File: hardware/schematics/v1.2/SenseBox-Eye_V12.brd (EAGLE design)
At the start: 61 x 25.4 mm, 103 parts, among them IC1 ESP32-S3-WROOM-1U-N16R8, IC2 WE-CHIP_ESP32-CAM, IC3 MCP73831T-2ACI/OT, IC5 AP2127N-2.8TRG1, IC6 AP2127N-1.5TRG1, IC7 REG710NA-5, IC8 MAX17048, IC9 RP602Z330C-E2-F, J1 USB-C-S, J2 U.FL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

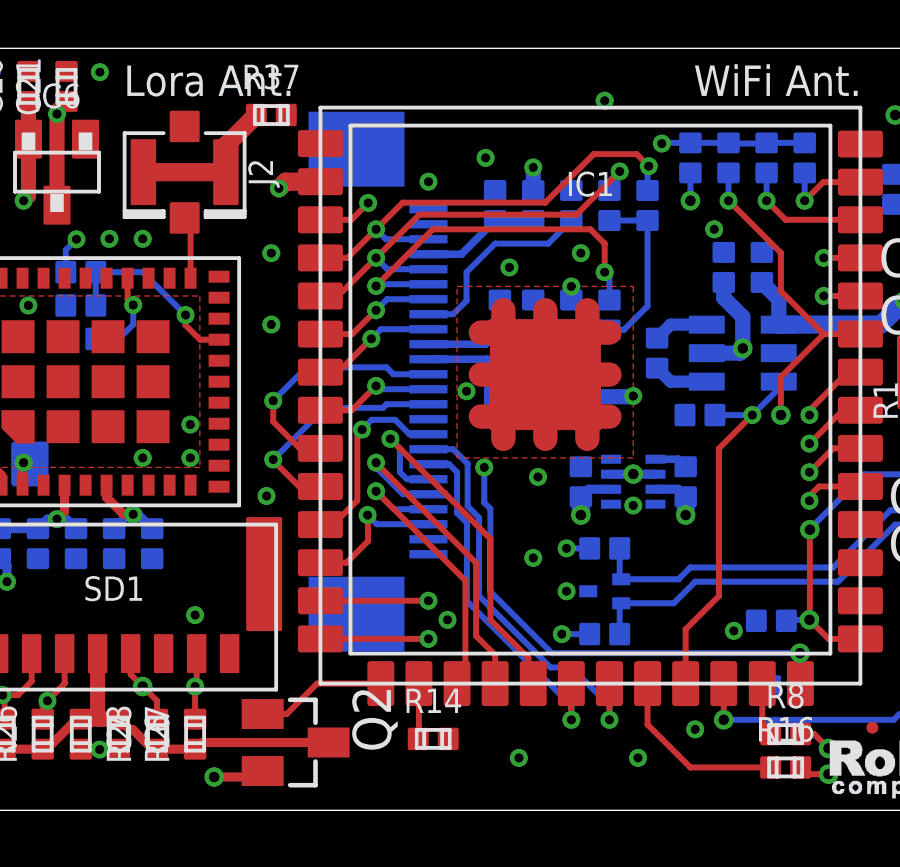
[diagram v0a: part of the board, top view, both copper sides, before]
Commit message: update v1.2 schematics
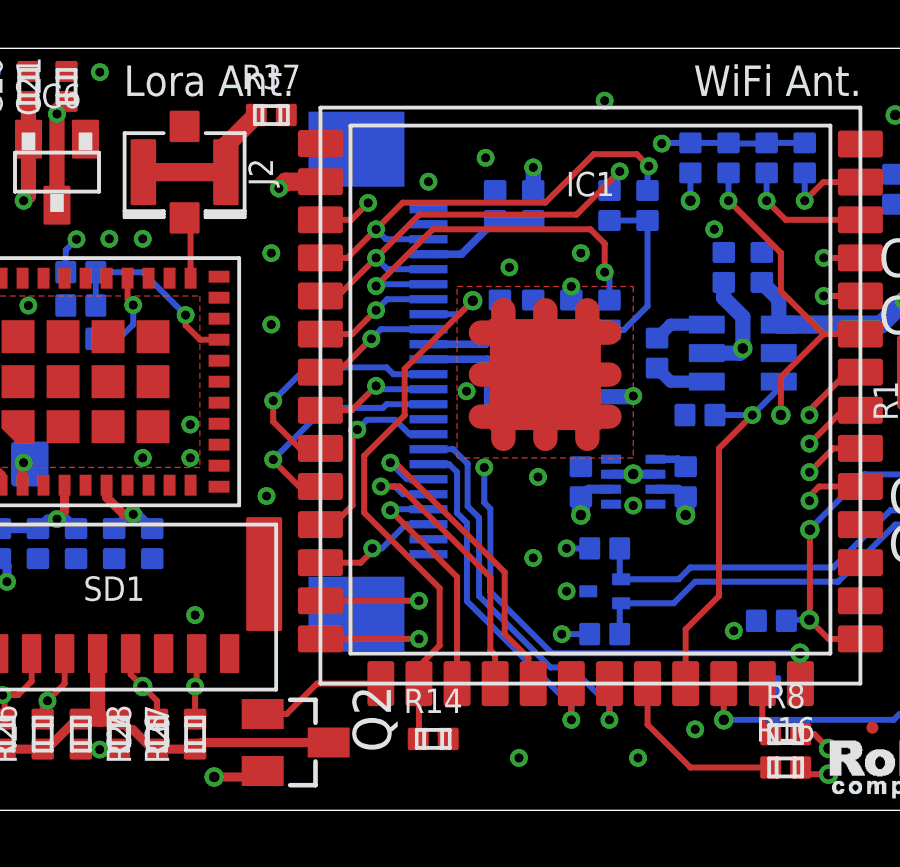
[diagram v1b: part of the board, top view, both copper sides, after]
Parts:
- removed R19: 10k, we-rcl:C0402
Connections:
- removed net IO46: IC1.16, R14.2
- net CAM_PWDN: now also IC1.16, R14.2; no longer R19.2
- net GND: no longer R19.1
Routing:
- net CAM_PWDN: track 6.61 -> 19.1 mm, vias 0 -> 1
- net IO46: track 1.85 -> 0.00 mm
- net CAM_Y3: track 9.75 -> 7.98 mm
- net CAM_Y2: track 12.4 -> 10.9 mm
- net CAM_Y5: track 11.3 -> 10.2 mm
- net CAM_Y4: track 4.92 -> 4.19 mm
- net GND: vias 53 -> 52
